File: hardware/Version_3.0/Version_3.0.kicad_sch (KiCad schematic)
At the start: 49 parts, among them J1 Conn_Coaxial, J2 Conn_Coaxial, J3 Conn_01x06_Pin, J4 Conn_01x06_Pin, J5 Conn_Coaxial, U1 ADF4351, Y1 SG-5032CAN

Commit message: Updated the hardware
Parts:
- removed J2, J5: Conn_Coaxial, Connector_Coaxial:SMA_Molex_73251-1153_EdgeMount_Horizontal, symbol Connector:Conn_Coaxial
- removed J3, J4: Conn_01x06_Pin, Connector_PinSocket_2.54mm:PinSocket_1x06_P2.54mm_Vertical, symbol Connector:Conn_01x06_Pin
- removed L4: 1.9nH, Inductor_SMD:L_0402_1005Metric, symbol Device:L
- removed R8: 0, Resistor_SMD:R_0402_1005Metric, symbol Device:R
- added J1, J2: Conn_01x05, Connector_PinHeader_2.54mm:PinHeader_1x05_P2.54mm_Vertical, symbol Connector_Generic:Conn_01x05
- R7: value DNI -> 50
- renumbered J1 to J3, R11 to R10, R9 to R8, R10 to R9
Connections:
- net +3.3V: now also J2.1 (Pin_1)
- net CE: now also J1.1 (Pin_1)
- net CLK: now also J1.4 (Pin_4)
- net CS: now also J1.2 (Pin_2)
- net GND: now also R7.2, J1.5 (Pin_5), J2.5 (Pin_5)
- net LD: now also J2.4 (Pin_4)
- net MOSI: now also J1.3 (Pin_3)
- net MUXOUT: now also J2.2 (Pin_2)
- net PDB_RF: now also J2.3 (Pin_3)
- net at R7.1: now also C17.1
- net at C15.1: now also Y1.3 (OUT); no longer R7.2
- net OUTA+: no longer names the net of J3.1 (In), L1.2
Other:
- note added: "- CLK, MOSI, and CS are the used for SPI programming of the chip. - CE is used to power on or off the chip. High is ON. - PDB_RF is used to control the output. High means there is an output. - LD is used to know when the VCO frequency is set. The chip makes this high when the frequency is set. - MUXOUT is used for a lot and can be programmed, check datasheet. - OUTA+ produce outputs of the VCO."
- note removed: "- CLK, MOSI, and CS are the used for SPI programming of the chip. - CE is used to power on or off the chip. High is ON. - PDB_RF is used to control the output. High means there is an output. - LD is used to know when the VCO frequency is set. The chip makes this high when the frequency is set. - MUXOUT is used for a lot and can be programmed, check datasheet. - OUTA+ and OUTA- produce outputs of 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"
- moved on the sheet: C11, C12, C13, C14, C17, J3, L1, L2, L3, Y1

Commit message: changed the pin header connectors for version 3 board
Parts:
- removed J1, J2: Conn_01x05, Connector_PinHeader_2.54mm:PinHeader_1x05_P2.54mm_Vertical, symbol Connector_Generic:Conn_01x05
- added J1: Conn_02x05_Counter_Clockwise, Connector_PinHeader_2.54mm:PinHeader_2x05_P2.54mm_Vertical, symbol Connector_Generic:Conn_02x05_Counter_Clockwise
- renumbered J3 to J2
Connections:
- net +3.3V: now also J1.1 (Pin_1)
- net CE: now also J1.2 (Pin_2)
- net CLK: now also J1.8 (Pin_8)
- net CS: now also J1.4 (Pin_4)
- net GND: now also J1.10 (Pin_10), J1.9 (Pin_9)
- net LD: now also J1.7 (Pin_7)
- net MOSI: now also J1.6 (Pin_6)
- net MUXOUT: now also J1.3 (Pin_3)
- net PDB_RF: now also J1.5 (Pin_5)
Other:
- title: ADF4351 Trial Board -> ADF4351 Board

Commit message: completed version 2 and version 3 pcb and production files completed
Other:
- title: ADF4351 Board -> ADF4351
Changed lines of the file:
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@@
 	(paper "A4")
 	(title_block
-		(title "ADF4351 Board")
+		(title "ADF4351")
 		(date "2026-09-28")
-		(rev "v1.0")
+		(rev "v3.0")
 		(comment 1 "by Dr Ekenedirichukwu Obianom")
 		(comment 3 "A fixed oscillator now sits there.")

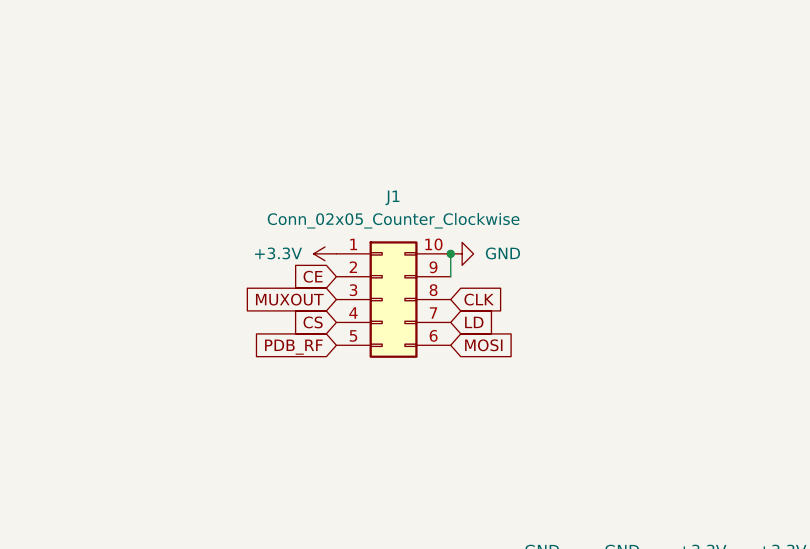
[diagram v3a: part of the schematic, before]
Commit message: Correct V3 header wiring and PCB routing
Update the Version 3 schematic and board with the corrected header pinout, ground connections, and signal routing. Refresh board figures and add PCBWay Gerber and IPC netlist production files.
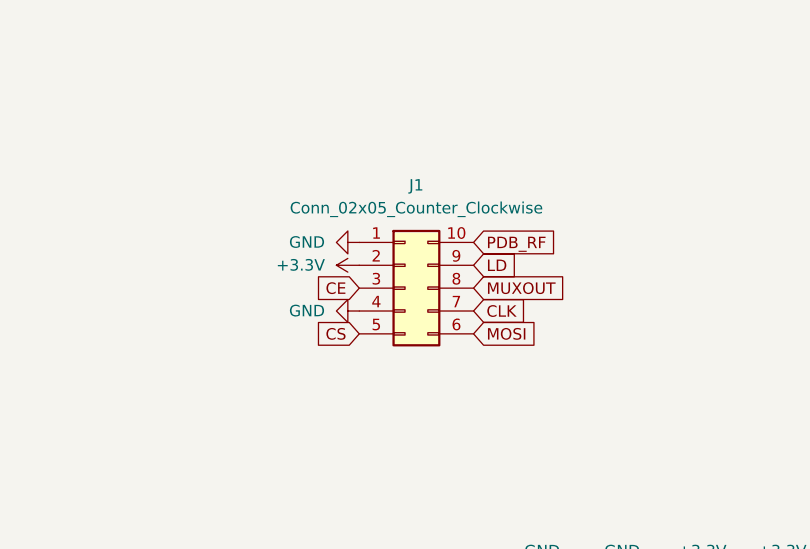
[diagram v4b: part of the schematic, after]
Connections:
- net +3.3V: now also J1.2 (Pin_2); no longer J1.1 (Pin_1)
- net CE: now also J1.3 (Pin_3); no longer J1.2 (Pin_2)
- net CLK: now also J1.7 (Pin_7); no longer J1.8 (Pin_8)
- net CS: now also J1.5 (Pin_5); no longer J1.4 (Pin_4)
- net GND: now also J1.1 (Pin_1), J1.4 (Pin_4); no longer J1.10 (Pin_10), J1.9 (Pin_9)
- net LD: now also J1.9 (Pin_9); no longer J1.7 (Pin_7)
- net MUXOUT: now also J1.8 (Pin_8); no longer J1.3 (Pin_3)
- net PDB_RF: now also J1.10 (Pin_10); no longer J1.5 (Pin_5)
